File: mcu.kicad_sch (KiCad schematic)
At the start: 14 parts, among them J2 Conn_01x10, J3 Conn_01x10, SW1 SW_Push, SW2 SW_Push, SW3 SW_Push, U3 ESP32-S3-WROOM-1

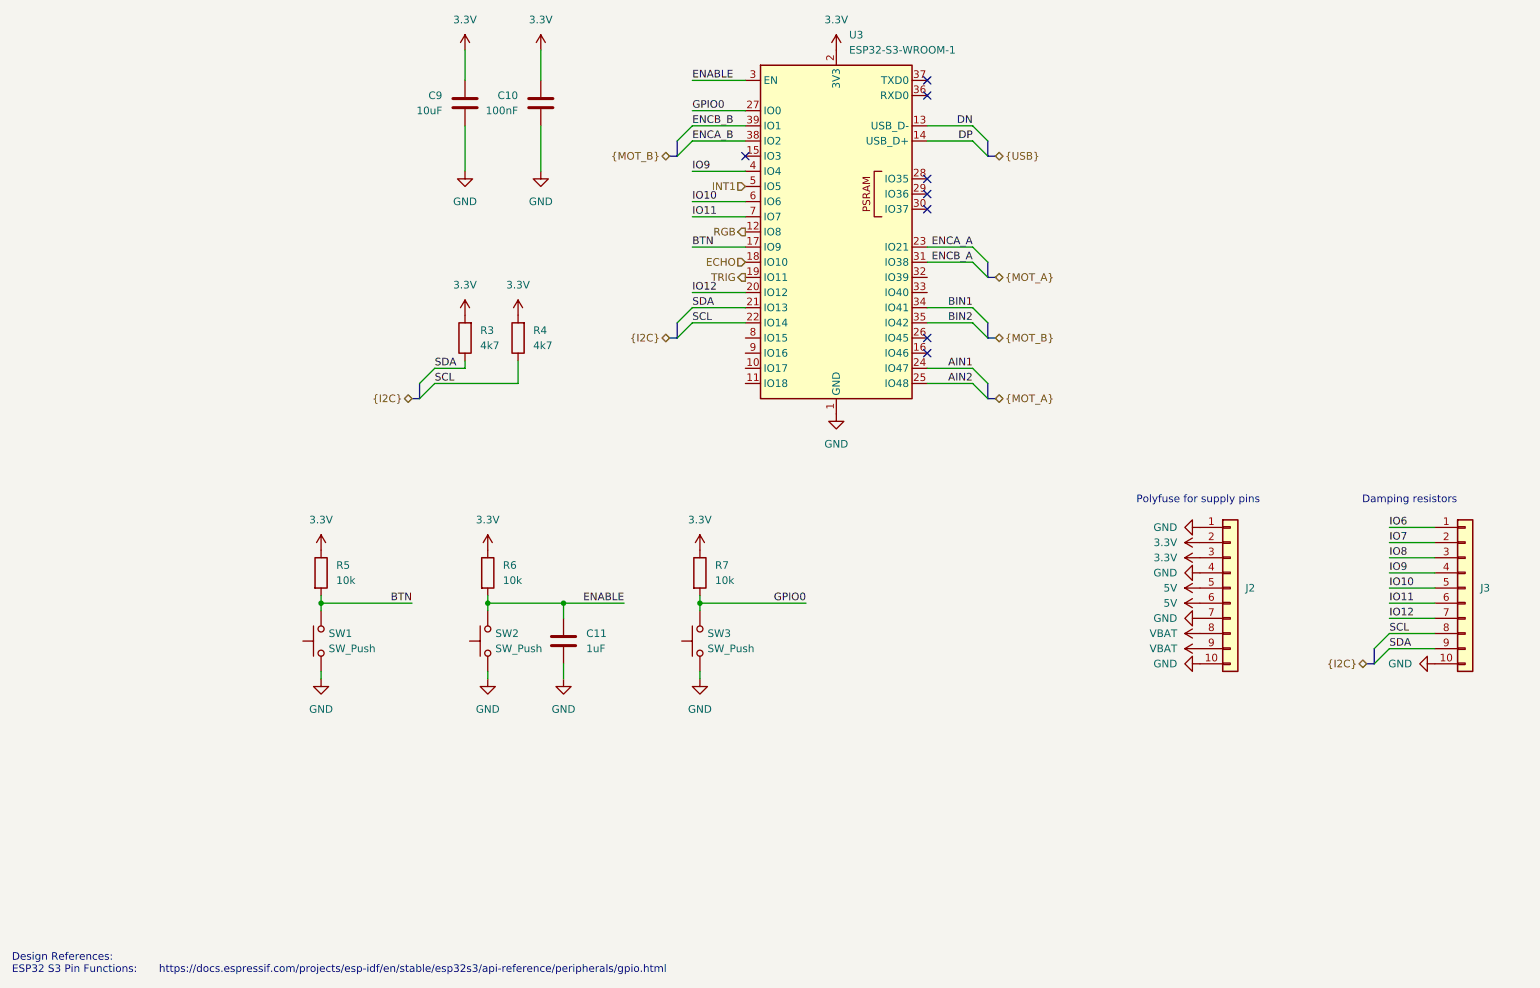
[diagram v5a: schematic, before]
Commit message: Continue layout and add pin header protection
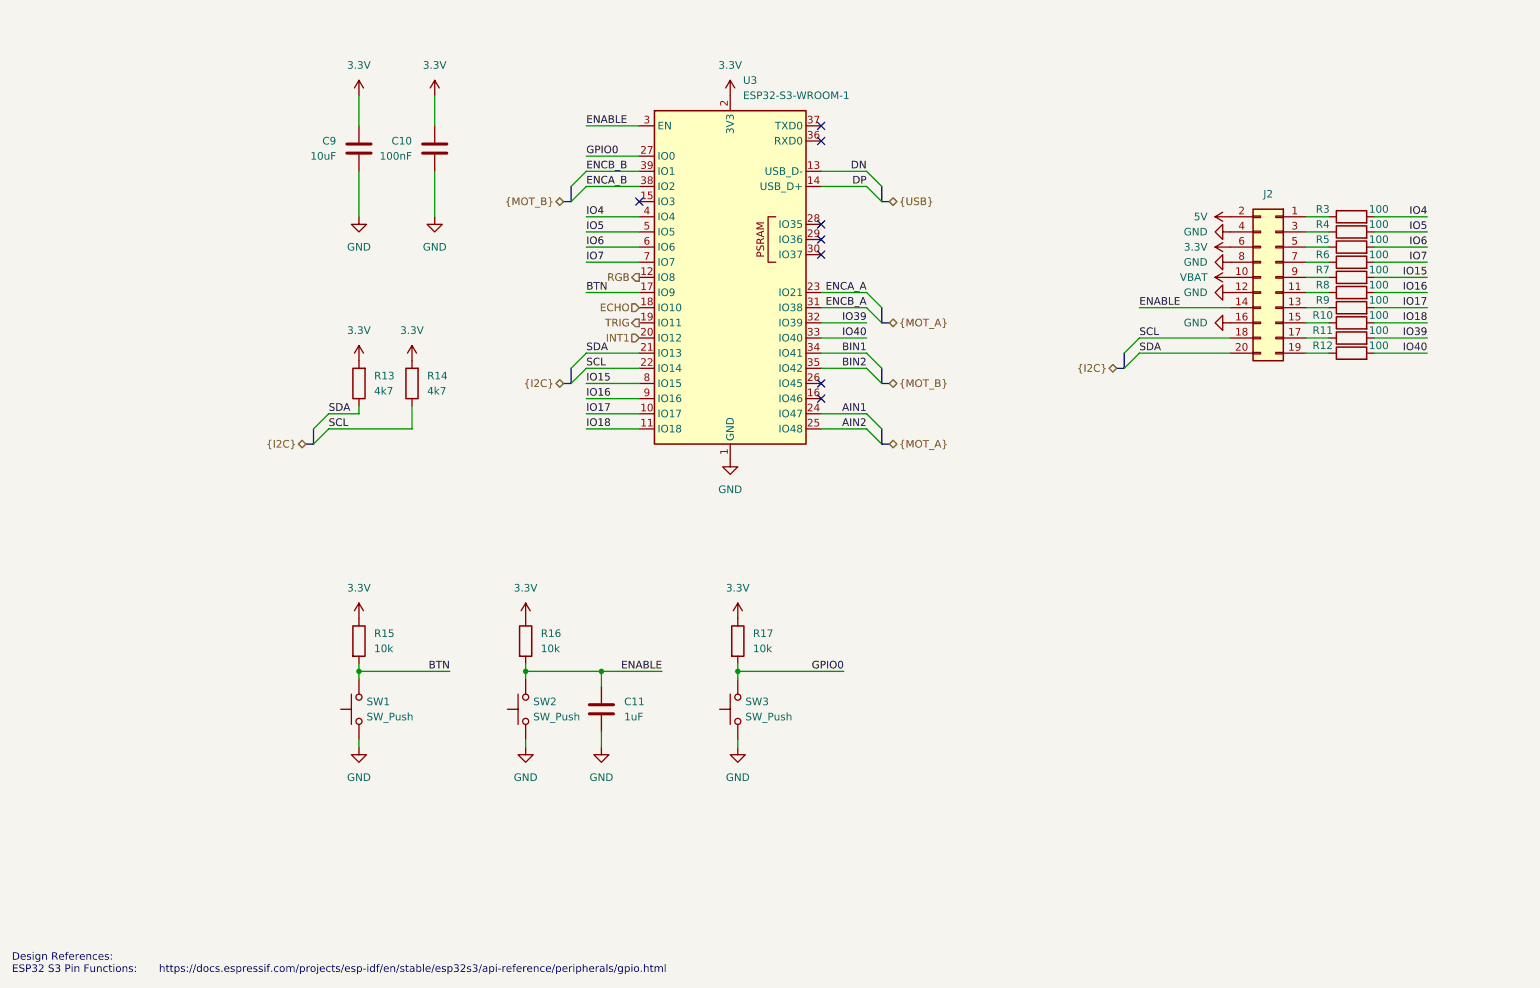
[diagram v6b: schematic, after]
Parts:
- removed J2, J3: Conn_01x10, Connector_PinHeader_2.54mm:PinHeader_1x10_P2.54mm_Vertical, symbol Connector_Generic:Conn_01x10
- added J2: Conn_02x10_Counter_Clockwise, Connector_PinHeader_2.54mm:PinHeader_2x10_P2.54mm_Vertical, symbol Connector_Generic:Conn_02x10_Odd_Even
- added R10, R11, R12, R3, R4, R5, R6, R7, R8, R9: 100, Resistor_SMD:R_0603_1608Metric, symbol Device:R
- renumbered R3 to R13, R4 to R14, R5 to R15, R6 to R16, R7 to R17
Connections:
- net IO10 is gone; now on net IO6: U3.6 (IO6)
- net IO11 is gone; now on net IO7: U3.7 (IO7)
- net IO12 is gone; now on net INT1: U3.20 (IO12)
- net 3.3V: now also J2.6 (Pin_6)
- net 5V: now also J2.2 (Pin_2)
- net ENABLE: now also J2.14 (Pin_14)
- net GND: now also J2.12 (Pin_12), J2.16 (Pin_16), J2.4 (Pin_4), J2.8 (Pin_8)
- net INT1: no longer U3.5 (IO5)
- net IO6: now also R5.2
- net IO7: now also R6.2
- net SCL: now also J2.18 (Pin_18)
- net SDA: now also J2.20 (Pin_20)
- net VBAT: now also J2.10 (Pin_10)
- net IO17: now reaches U3.10 (IO17)
- net IO17: now also R9.2
- net IO18: now reaches U3.11 (IO18)
- net IO18: now also R10.2
- net IO39: now reaches U3.32 (IO39)
- net IO39: now also R11.2
- net IO40: now reaches U3.33 (IO40)
- net IO40: now also R12.2
- net IO15: now reaches U3.8 (IO15)
- net IO15: now also R7.2
- net IO16: now reaches U3.9 (IO16)
- net IO16: now also R8.2
- net IO9 renamed IO4
- net IO4: now also R3.2
- new net: J2.15 (Pin_15), R10.1
- new net: J2.9 (Pin_9), R7.1
- new net: J2.3 (Pin_3), R4.1
- new net: J2.7 (Pin_7), R6.1
- new net: J2.1 (Pin_1), R3.1
- new net: J2.11 (Pin_11), R8.1
- new net: J2.13 (Pin_13), R9.1
- new net: J2.17 (Pin_17), R11.1
- new net: J2.19 (Pin_19), R12.1
- new net: J2.5 (Pin_5), R5.1
- new net IO5: R4.2, U3.5 (IO5)
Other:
- note removed: "Damping resistors"
- note removed: "Polyfuse for supply pins"
- moved on the sheet: C10, C11, C9, R13, R14, R15, R16, R17, SW1, SW2, SW3, U3

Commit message: Add linesensor pin header
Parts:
- added J7: Conn_01x11, Connector_PinHeader_2.54mm:PinHeader_1x11_P2.54mm_Vertical, symbol Connector_Generic:Conn_01x11
- added J8: Conn_01x08, Connector_PinHeader_2.54mm:PinHeader_1x08_P2.54mm_Vertical, symbol Connector_Generic:Conn_01x08
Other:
- moved on the sheet: J2, R10, R11, R12, R3, R4, R5, R6, R7, R8, R9

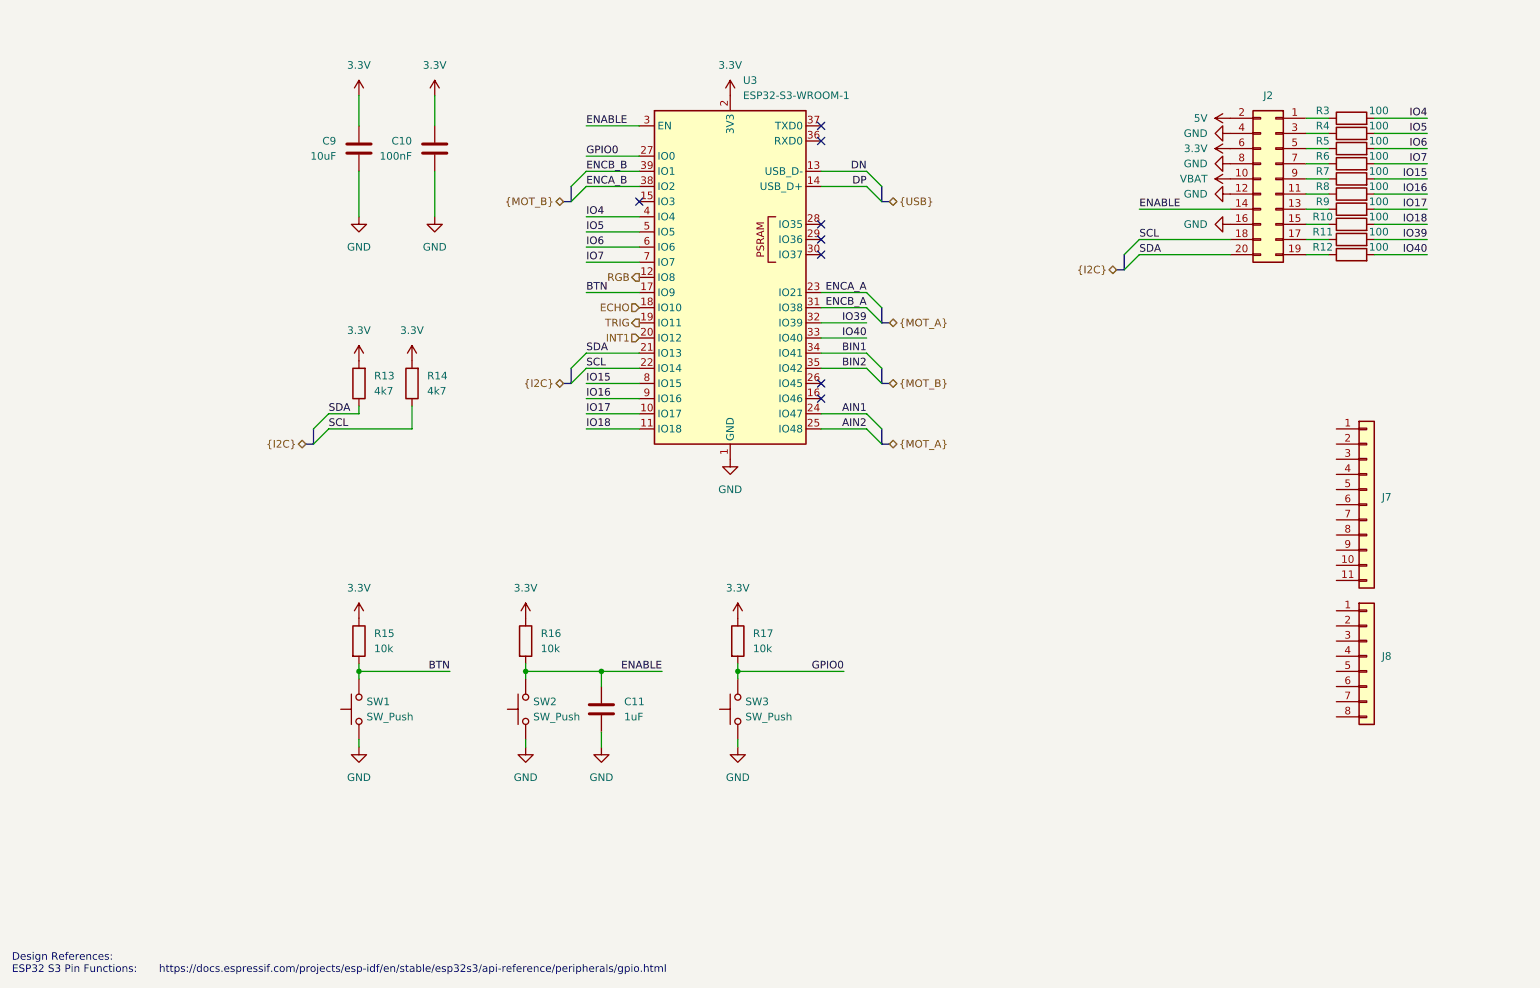
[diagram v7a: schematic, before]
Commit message: Document strapping pins
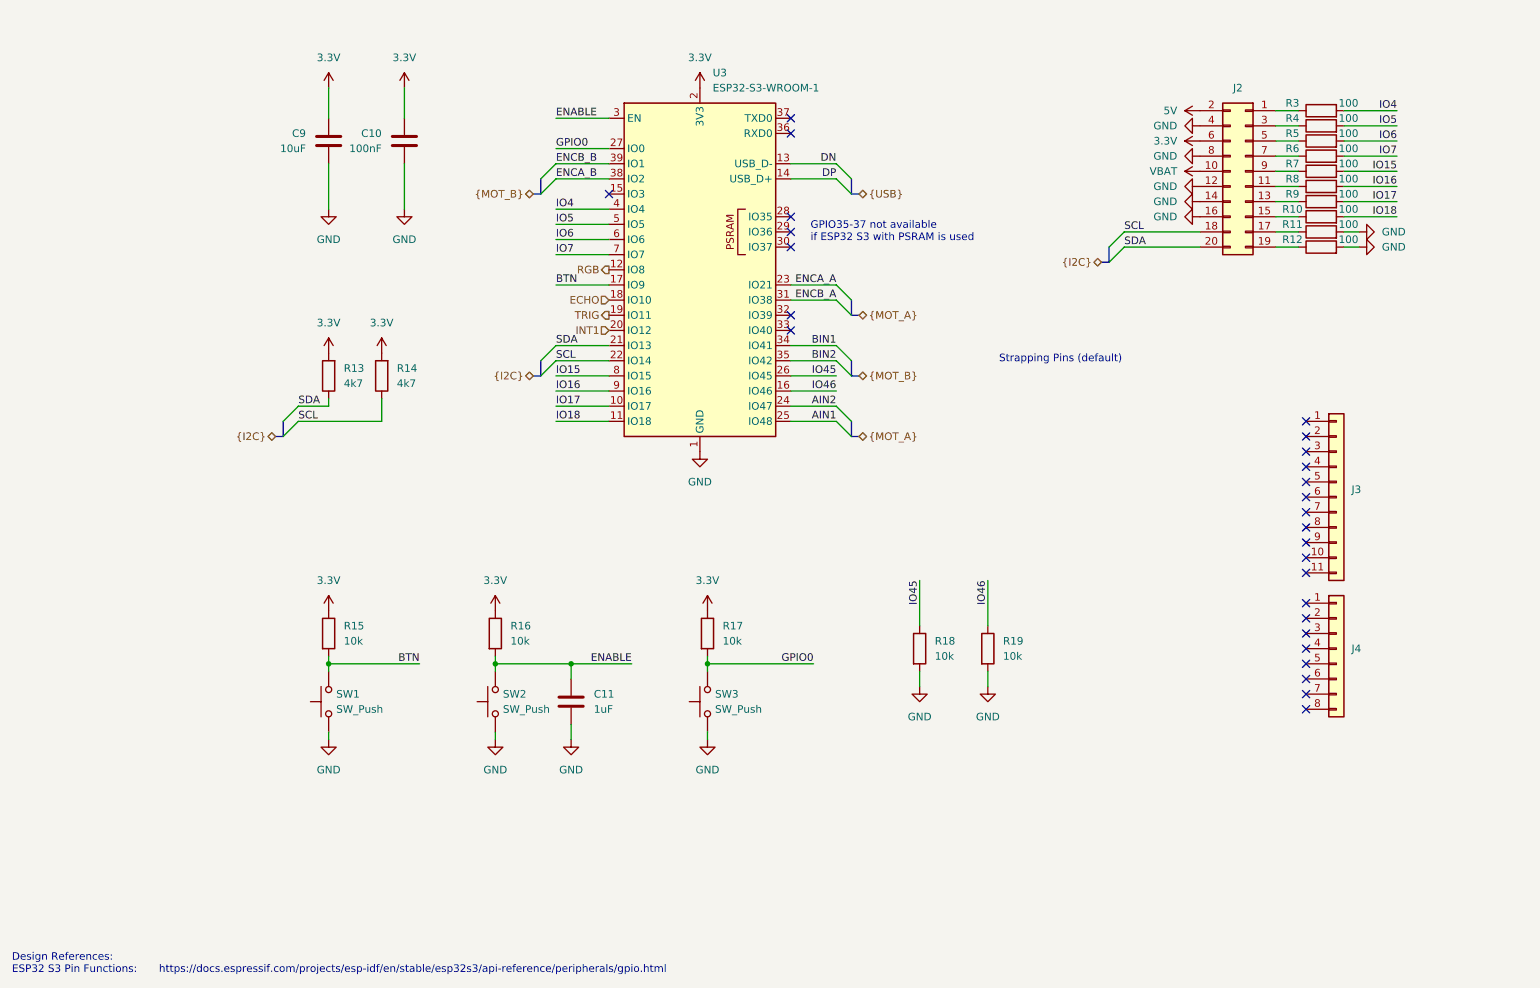
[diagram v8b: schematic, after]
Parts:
- added R18, R19: 10k, Resistor_SMD:R_0603_1608Metric, symbol Device:R
- renumbered J7 to J3, J8 to J4
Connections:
- net AIN1: now also U3.25 (IO48); no longer U3.24 (IO47)
- net AIN2: now also U3.24 (IO47); no longer U3.25 (IO48)
- net ENABLE: no longer J2.14 (Pin_14)
- net GND: now also J2.14 (Pin_14), R11.2, R12.2, R18.2, R19.2
- net IO46: now reaches U3.16 (IO46)
- net IO46: now also R19.1
- net IO45: now reaches U3.26 (IO45)
- net IO45: now also R18.1
- net IO39: no longer names the net of U3.32 (IO39)
- net IO39: no longer R11.2
- net IO40: no longer names the net of U3.33 (IO40)
- net IO40: no longer R12.2
- no-connect marks 8 -> 27
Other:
- note added: "GPIO35-37 not available if ESP32 S3 with PSRAM is used"
- note added: "Strapping Pins (default)"
- moved on the sheet: C10, C11, C9, J2, J3, J4, R10, R11, R12, R13, R14, R15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
